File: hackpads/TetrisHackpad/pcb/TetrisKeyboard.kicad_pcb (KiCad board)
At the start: 2 copper layers, 100 x 100 mm, 31 parts, among them SW1 CherryMX_1.00u_KailhSocket, SW10 CherryMX_1.00u_KailhSocket, SW2 CherryMX_1.00u_KailhSocket, SW3 CherryMX_1.00u_KailhSocket, SW4 CherryMX_1.00u_KailhSocket, SW5 CherryMX_1.00u_KailhSocket, SW6 CherryMX_1.00u_KailhSocket, SW7 CherryMX_1.00u_KailhSocket, SW8 CherryMX_1.00u_KailhSocket, SW9 CherryMX_1.00u_KailhSocket

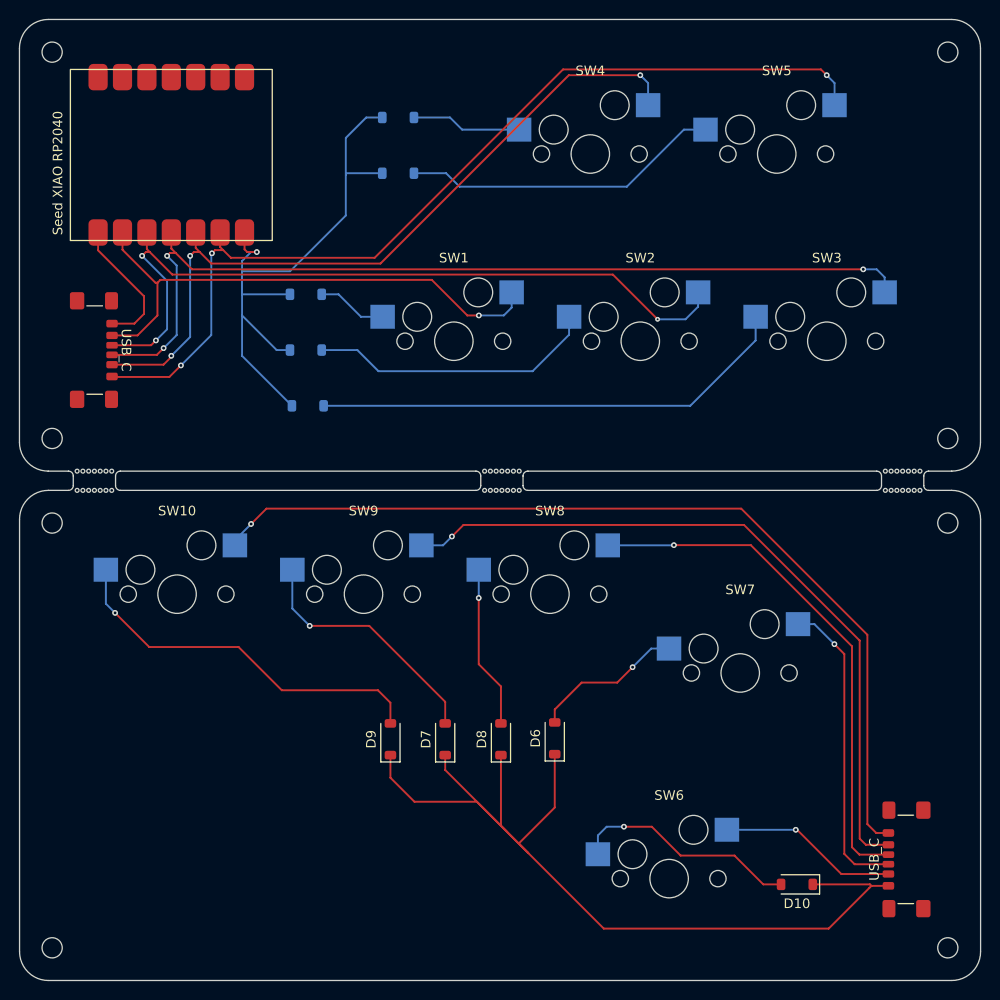
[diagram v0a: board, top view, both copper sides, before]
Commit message: Update PCB
Add backup pads in case USB C doesn't work
Add new silkscreens
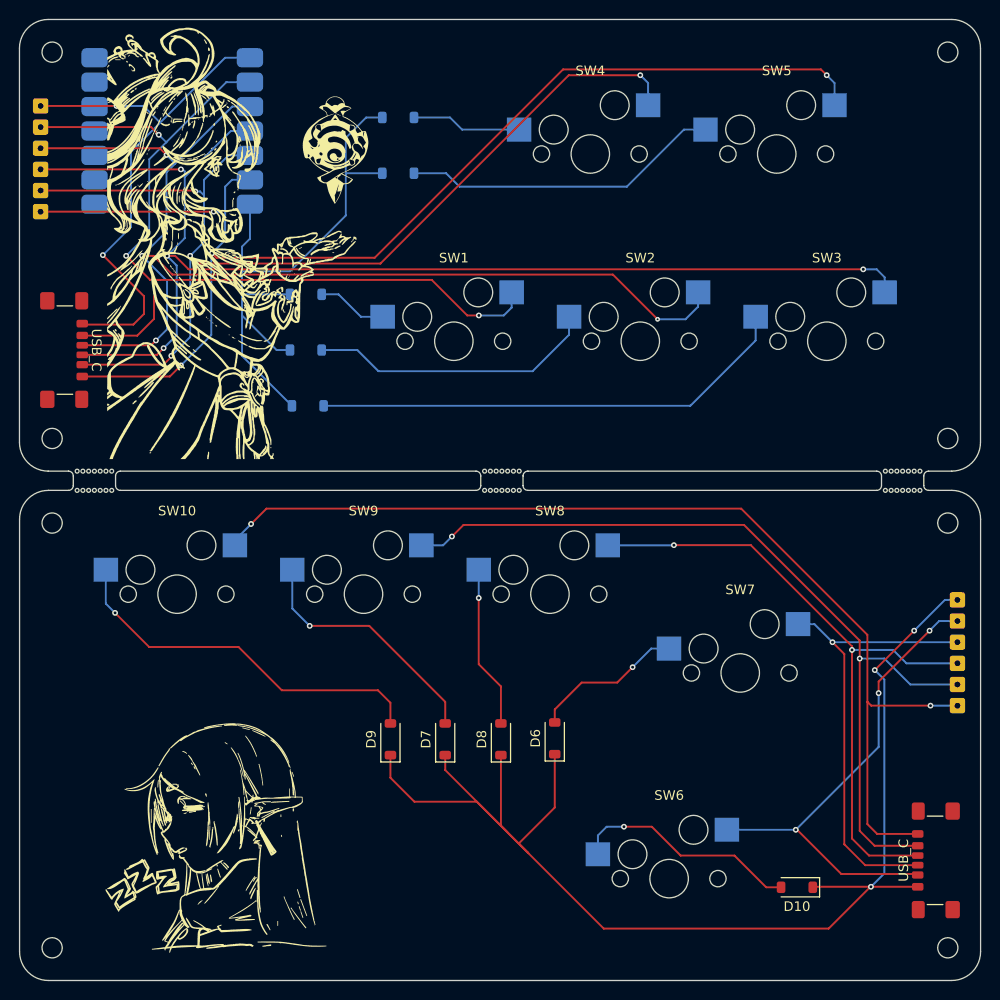
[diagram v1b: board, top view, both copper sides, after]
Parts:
- added ?: , , F.Cu at (20.8, 47.4)
- added ?: , , F.Cu at (20.8, 49.6)
- added ?: , , F.Cu at (116.2, 101.0)
- added ?: , , F.Cu at (116.2, 103.2)
- added ?: , , F.Cu at (116.2, 92.2)
- added ?: , , F.Cu at (20.8, 51.8)
- added ?: , , F.Cu at (116.2, 94.4)
- added ?: , , F.Cu at (20.8, 45.2)
- added ?: , , F.Cu at (20.8, 43.0)
- added ?: , , F.Cu at (116.2, 96.6)
- added ?: , , F.Cu at (116.2, 98.8)
- added G***: LOGO, LOGO, F.Cu at (41.2, 53.6)
- added G***: LOGO, LOGO, F.Cu at (51.5, 45.4)
- added NO: LOGO, LOGO, F.Cu at (39.8, 117.3)
- added REF**: SolderWire-0.1sqmm_1x01_D0.4mm_OD1mm, Connector_Wire:SolderWire-0.1sqmm_1x01_D0.4mm_OD1mm, F.Cu at (20.8, 40.8)
- Seed XIAO RP2040: moved to B.Cu
- moved USB_C 3.10 mm to (22.1, 66.2)
- moved USB_C 3.05 mm to (115.1, 119.3)
- moved Seed XIAO RP2040 1.73 mm to (43.4, 53.9), turned to 180 degrees
- moved D10 0.30 mm to (99.5, 122.1)
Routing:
- net Row2: track 14.2 -> 56.3 mm, vias 0 -> 2
- net Col1: track 56.3 -> 96.0 mm, vias 1 -> 3
- net Row2-B: track 225.5 -> 263.5 mm, vias 5 -> 8
- net Col2: track 80.2 -> 116.7 mm, vias 3 -> 4
- net Col3: track 96.0 -> 129.8 mm, vias 3 -> 4
- net Col1-B: track 18.7 -> 51.5 mm, vias 1 -> 3
- net Col4: track 79.2 -> 111.2 mm, vias 3 -> 4
- net Col5: track 98.9 -> 129.6 mm, vias 3 -> 4
- net Col2-B: track 31.9 -> 47.4 mm
- net Col3-B: track 54.8 -> 68.9 mm, vias 1 -> 2
- net Col4-B: track 75.3 -> 89.2 mm, vias 1 -> 2
- net Col5-B: track 94.6 -> 107.5 mm, vias 1 -> 2
- net Row1: track 198.0 -> 199.1 mm, vias 1 -> 0
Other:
- board text added: "Tetris Keyboard By DeadHello and Jayx2u"
- board text removed: "22/09/24"
- board text removed: "Tetris Keyboard"

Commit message: Move RP2040 and USB C ports, update silkscreens
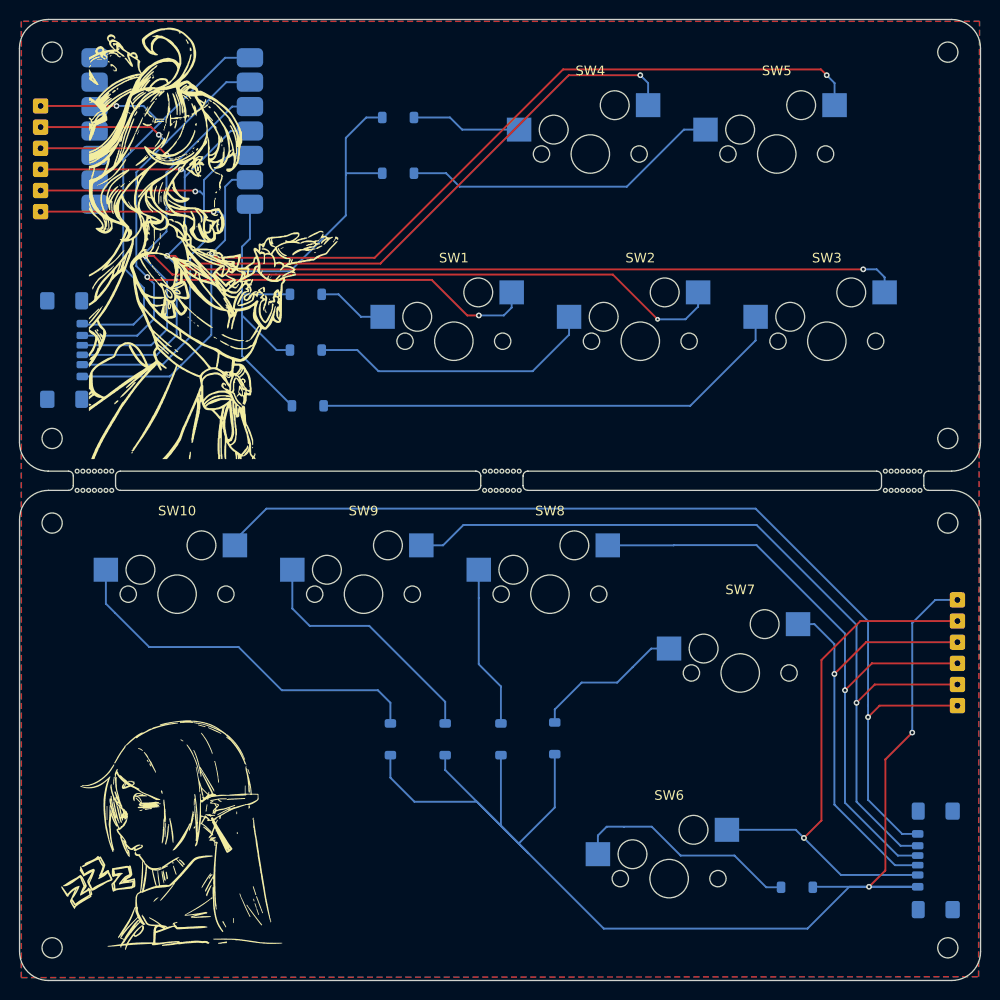
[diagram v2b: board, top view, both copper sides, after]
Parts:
- added G***: LOGO, LOGO, F.Cu at (61.9, 116.8)
- added G***: LOGO, LOGO, B.Cu at (43.3, 122.8)
- added G***: LOGO, LOGO, B.Cu at (35.7, 66.2)
- D10, D6, D7, D8, D9, USB_C (x2): moved to B.Cu
- moved NO 4.61 mm to (35.2, 117.0)
- moved G*** 1.90 mm to (39.3, 53.6)
- turned D10 to 0 degrees
- turned USB_C to 90 degrees
- turned USB_C to -90 degrees
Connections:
- Seed XIAO RP2040 pad 13: (no net) -> GND
- USB_C pad A12: Col5 -> Row2
- USB_C pad A5: Col2 -> Col3
- USB_C pad A9: Col4 -> Col1
- USB_C pad B12: Row2 -> Col5
- USB_C pad B5: Col3 -> Col2
- USB_C pad B9: Col1 -> Col4
- USB_C pad A12: Col5-B -> Row2-B
- USB_C pad A5: Col2-B -> Col3-B
- USB_C pad A9: Col4-B -> Col1-B
- USB_C pad B12: Row2-B -> Col5-B
- USB_C pad B5: Col3-B -> Col2-B
- USB_C pad B9: Col1-B -> Col4-B
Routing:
- net Col1-B: track 51.5 -> 56.9 mm, vias 3 -> 1
- net Row2-B: track 263.5 -> 266.9 mm, vias 8 -> 2
- net Row2: track 56.3 -> 54.6 mm, vias 2 -> 1
- net Col1: track 96.0 -> 95.1 mm
- net Col4-B: track 89.2 -> 88.4 mm, vias 2 -> 1
- net Col2-B: track 47.4 -> 46.8 mm
- net Col2: track 116.7 -> 116.1 mm, vias 4 -> 3
- net Col5-B: track 107.5 -> 107.1 mm, vias 2 -> 1
- net Col4: track 111.2 -> 111.0 mm, vias 4 -> 3
- net Col3-B: track 68.9 -> 68.8 mm, vias 2 -> 1
- net Col5: vias 4 -> 3
- net Col3: vias 4 -> 3
- added copper zone on B.Cu, net GND
- added copper zone on F.Cu, net GND
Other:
- board text added: "Tetris Keyboard v1.3 Designed by DeadHello and Jayx2u"
- board text removed: "Tetris Keyboard By DeadHello and Jayx2u"

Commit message: Slightly shift components
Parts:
- moved G*** 1.22 mm to (50.8, 44.4)
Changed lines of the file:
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@@
 	(footprint "LOGO"
 		(layer "F.Cu")
-		(at 51.5 45.4)
+		(at 50.8 44.4)
 		(property "Reference" "G***"
 			(at 0 0 0)
